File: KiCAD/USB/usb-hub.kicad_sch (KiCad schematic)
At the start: 22 parts, among them J1 046809610110846+ Male, J2 046809610110846+ Female, J3 Conn_01x04_Socket, U1 CY7C65634-28LTXC, Y1 12MHz 20pF

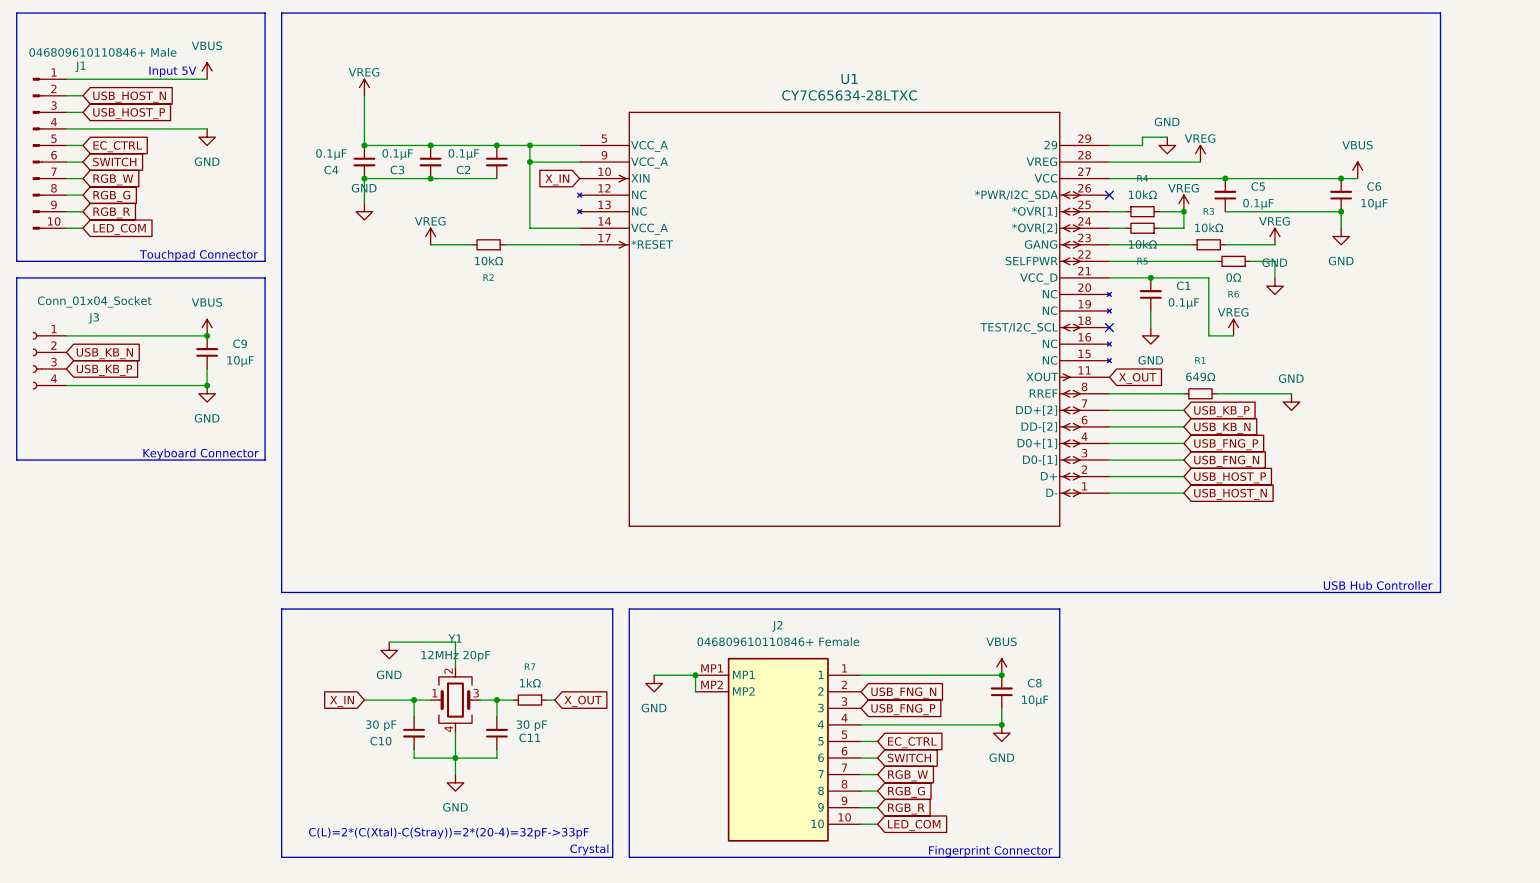
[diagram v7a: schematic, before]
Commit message: ofc i had to be using the wrong footprint
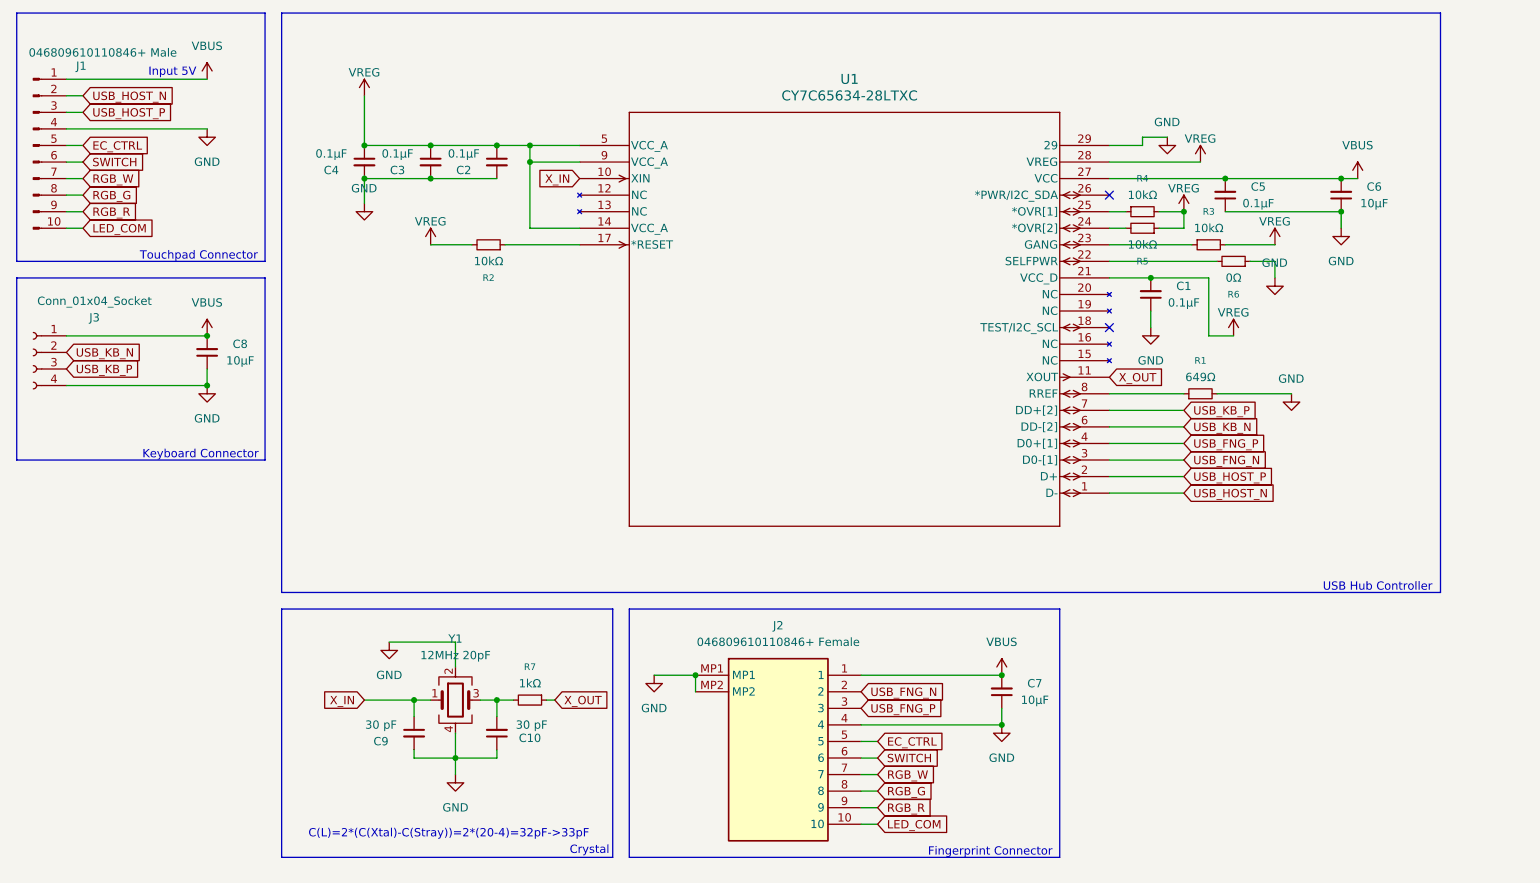
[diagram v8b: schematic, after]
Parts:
- C1, C2, C3, C4, C5, C6: footprint Capacitor_SMD:C_01005_0402Metric -> Capacitor_SMD:C_0402_1005Metric
- C10: renamed from C11; footprint Capacitor_SMD:C_01005_0402Metric -> Capacitor_SMD:C_0402_1005Metric
- C7: renamed from C8; footprint Capacitor_SMD:C_01005_0402Metric -> Capacitor_SMD:C_0402_1005Metric
- C8: renamed from C9; footprint Capacitor_SMD:C_01005_0402Metric -> Capacitor_SMD:C_0402_1005Metric
- C9: renamed from C10; footprint Capacitor_SMD:C_01005_0402Metric -> Capacitor_SMD:C_0402_1005Metric
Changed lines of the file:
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@@
 			)
 		)
-		(property "Footprint" "Capacitor_SMD:C_01005_0402Metric"
+		(property "Footprint" "Capacitor_SMD:C_0402_1005Metric"
 			(at 88.9 48.26 0)
 			(effects
@@
 		(on_board yes)
 		(dnp no)
-		(property "Reference" "C9"
+		(property "Reference" "C8"
 			(at 59.6837 76.2 0)
 			(effects
@@
 			)
 		)
-		(property "Footprint" "Capacitor_SMD:C_01005_0402Metric"
+		(property "Footprint" "Capacitor_SMD:C_0402_1005Metric"
 			(at 54.61 77.47 0)
 			(effects
@@
 			(project "usb-hub"
 				(path "/215ab3b1-85fe-4e4f-901d-105bf68c1066"
-					(reference "C9")
+					(reference "C8")
 					(unit 1)
 				)
@@
 		(on_board yes)
 		(dnp no)
-		(property "Reference" "C10"
+		(property "Reference" "C9"
 			(at 81.2863 137.16 0)
 			(effects
@@
 			)
 		)
-		(property "Footprint" "Capacitor_SMD:C_01005_0402Metric"
+		(property "Footprint" "Capacitor_SMD:C_0402_1005Metric"
 			(at 86.36 135.89 0)
 			(effects
@@
 			(project "usb-hub"
 				(path "/215ab3b1-85fe-4e4f-901d-105bf68c1066"
-					(reference "C10")
+					(reference "C9")
 					(unit 1)
 				)
@@
 		(on_board yes)
 		(dnp no)
-		(property "Reference" "C11"
+		(property "Reference" "C10"
 			(at 104.14 136.652 0)
 			(effects
@@
 			)
 		)
-		(property "Footprint" "Capacitor_SMD:C_01005_0402Metric"
+		(property "Footprint" "Capacitor_SMD:C_0402_1005Metric"
 			(at 99.06 135.89 0)
 			(effects
@@
 			(project "usb-hub"
 				(path "/215ab3b1-85fe-4e4f-901d-105bf68c1066"
-					(reference "C11")
+					(reference "C10")
 					(unit 1)
 				)
@@
 			)
 		)
-		(property "Footprint" "Capacitor_SMD:C_01005_0402Metric"
+		(property "Footprint" "Capacitor_SMD:C_0402_1005Metric"
 			(at 99.06 48.26 0)
 			(effects
@@
 			)
 		)
-		(property "Footprint" "Capacitor_SMD:C_01005_0402Metric"
+		(property "Footprint" "Capacitor_SMD:C_0402_1005Metric"
 			(at 228.6 53.34 0)
 			(effects
@@
 			)
 		)
-		(property "Footprint" "Capacitor_SMD:C_01005_0402Metric"
+		(property "Footprint" "Capacitor_SMD:C_0402_1005Metric"
 			(at 210.82 53.34 0)
 			(effects
@@
 			)
 		)
-		(property "Footprint" "Capacitor_SMD:C_01005_0402Metric"
+		(property "Footprint" "Capacitor_SMD:C_0402_1005Metric"
 			(at 78.74 48.26 0)
 			(effects
@@
 		(on_board yes)
 		(dnp no)
-		(property "Reference" "C8"
+		(property "Reference" "C7"
 			(at 181.6037 128.27 0)
 			(effects
@@
 			)
 		)
-		(property "Footprint" "Capacitor_SMD:C_01005_0402Metric"
+		(property "Footprint" "Capacitor_SMD:C_0402_1005Metric"
 			(at 176.53 129.54 0)
 			(effects
@@
 			(project "usb-hub"
 				(path "/215ab3b1-85fe-4e4f-901d-105bf68c1066"
-					(reference "C8")
+					(reference "C7")
 					(unit 1)
 				)
@@
 			)
 		)
-		(property "Footprint" "Capacitor_SMD:C_01005_0402Metric"
+		(property "Footprint" "Capacitor_SMD:C_0402_1005Metric"
 			(at 199.39 68.58 0)
 			(effects
